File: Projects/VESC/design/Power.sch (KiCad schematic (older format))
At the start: 48 parts, among them U2 TC2117, U3 DRV8302

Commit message: More schematic updates for VESC
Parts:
- C1, C18, C19, C20, C21, C22, C23, C24, C26, C27, C28, C29, C30, C34, C36, C37, C39, C40, C43, C44, C49, C51, C52, C8, C9: symbol C-RESCUE-BLDC_4 -> C
- C25, C33: symbol CP1-RESCUE-BLDC_4 -> CP1
- D4: symbol DIODESCH -> D_Schottky
- D5: symbol DIODE -> D
- R17, R18, R19, R20, R21, R23, R24, R25, R26, R27, R32, R33, R48, R49, R50, R51: symbol R-RESCUE-BLDC_4 -> R
- U2: symbol NCP1117ST33T3G-RESCUE-BLDC_4 -> NCP1117ST33T3G
- U3: symbol DRV8302 -> DRV8302_1
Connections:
- net +5V: no longer U2.3 (VI)
- net GND: no longer U2.1 (GND)
- net VCC: no longer U2.2 (VO)
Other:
- moved on the sheet: U2

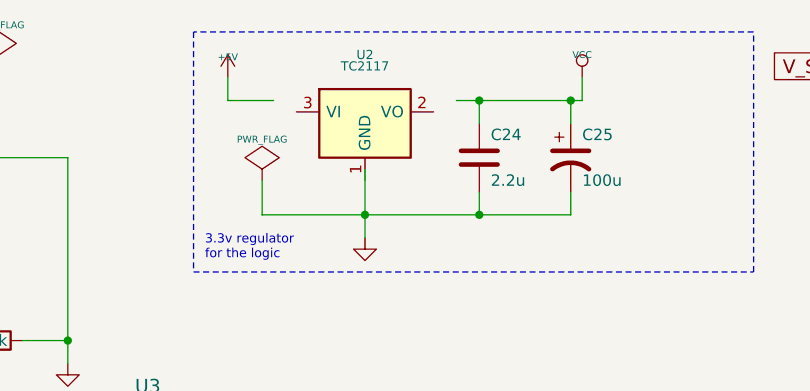
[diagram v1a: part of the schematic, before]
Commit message: VESC MOSFET layout
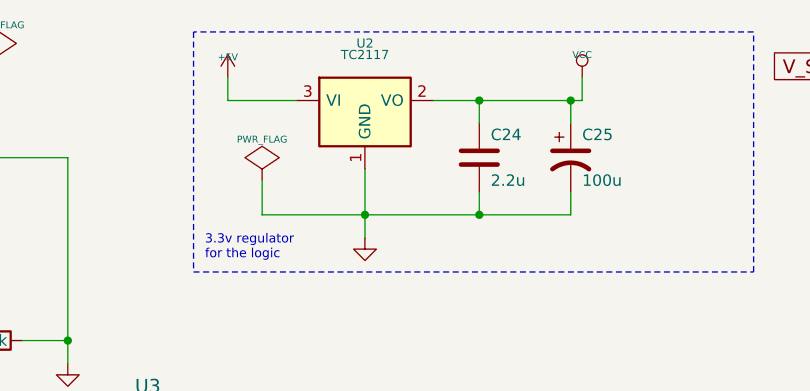
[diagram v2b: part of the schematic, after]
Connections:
- net +5V: now also U2.3 (VI)
- net GND: now also U2.1 (GND)
- net VCC: now also U2.2 (VO)
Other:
- moved on the sheet: U2
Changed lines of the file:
@@
 L NCP1117ST33T3G U2
 U 1 1 53E7AF36
-P 6300 1200
+P 6300 1150
 AR Path="/53E7AF36" Ref="U2"  Part="1"
 AR Path="/504F83BE/53E7AF36" Ref="U2"  Part="1"
-F 0 "U2" H 6300 1450 40  0000 C CNN
-F 1 "TC2117" H 6300 1400 40  0000 C CNN
-F 2 "CRF1:SOT-223" H 6300 1200 60  0001 C CNN
-F 3 "" H 6300 1200 60  0000 C CNN
-	1    6300 1200
+F 0 "U2" H 6300 1400 40  0000 C CNN
+F 1 "TC2117" H 6300 1350 40  0000 C CNN
+F 2 "CRF1:SOT-223" H 6300 1150 60  0001 C CNN
+F 3 "" H 6300 1150 60  0000 C CNN
+	1    6300 1150
 	1    0    0    -1
 $EndComp
@@
 0D 0D 85 50 5B 08 A1 71 E3 C6 45 47 47 77 AB F8 CD C0 F0 65 C3 18 9A 0F 4F 4B 4B 4B 51 51 51 53
 53 93 40 20 30 31 31 61 94 40 19 18 18 43 C3 C0 C0 A0 72 FE 07 CF 64 8C 61 E1 12 74 DD 00 00 00
-00 49 45 4E 44 AE 42 60 82 02
+00 49 45 4E 44 AE 42 60 82 17
 EndData
 $EndBitmap
@@
 A1 C7 18 00 00 C0 28 C8 B2 00 00 00 46 41 96 05 00 00 30 0A B2 2C 00 00 80 51 90 65 01 00 00 8C
 82 2C 0B 00 00 60 14 64 59 00 00 00 A3 FC 7F BD 9B 69 A6 C1 67 F0 EA 00 00 00 00 49 45 4E 44 AE
-42 60 82 37
+42 60 82 D7
 EndData
 $EndBitmap
@@
 AB D8 39 0B 59 91 9E DF A8 2A 5B EE 54 3A FD 71 ED 71 2F 29 C3 82 EC 80 87 06 6E C3 98 10 30 3B
 62 9A BB 2D 03 B8 C4 64 FC B5 26 AC 13 9B D1 39 40 41 C1 D6 78 4C 84 BF 94 F0 6F E1 BF 96 F0 0F
-FF 77 E2 FF 1F 0F 43 55 32 21 1C 08 16 00 00 00 00 49 45 4E 44 AE 42 60 82 0B
+FF 77 E2 FF 1F 0F 43 55 32 21 1C 08 16 00 00 00 00 49 45 4E 44 AE 42 60 82 04
 EndData
 $EndBitmap
@@
 Connection ~ 7200 1150
 Wire Wire Line
-	6700 1150 7250 1150
+	6600 1150 7250 1150
 Wire Wire Line
-	5900 1150 5700 1150
+	5700 1150 6000 1150
 Wire Wire Line
 	5700 1150 5700 1050

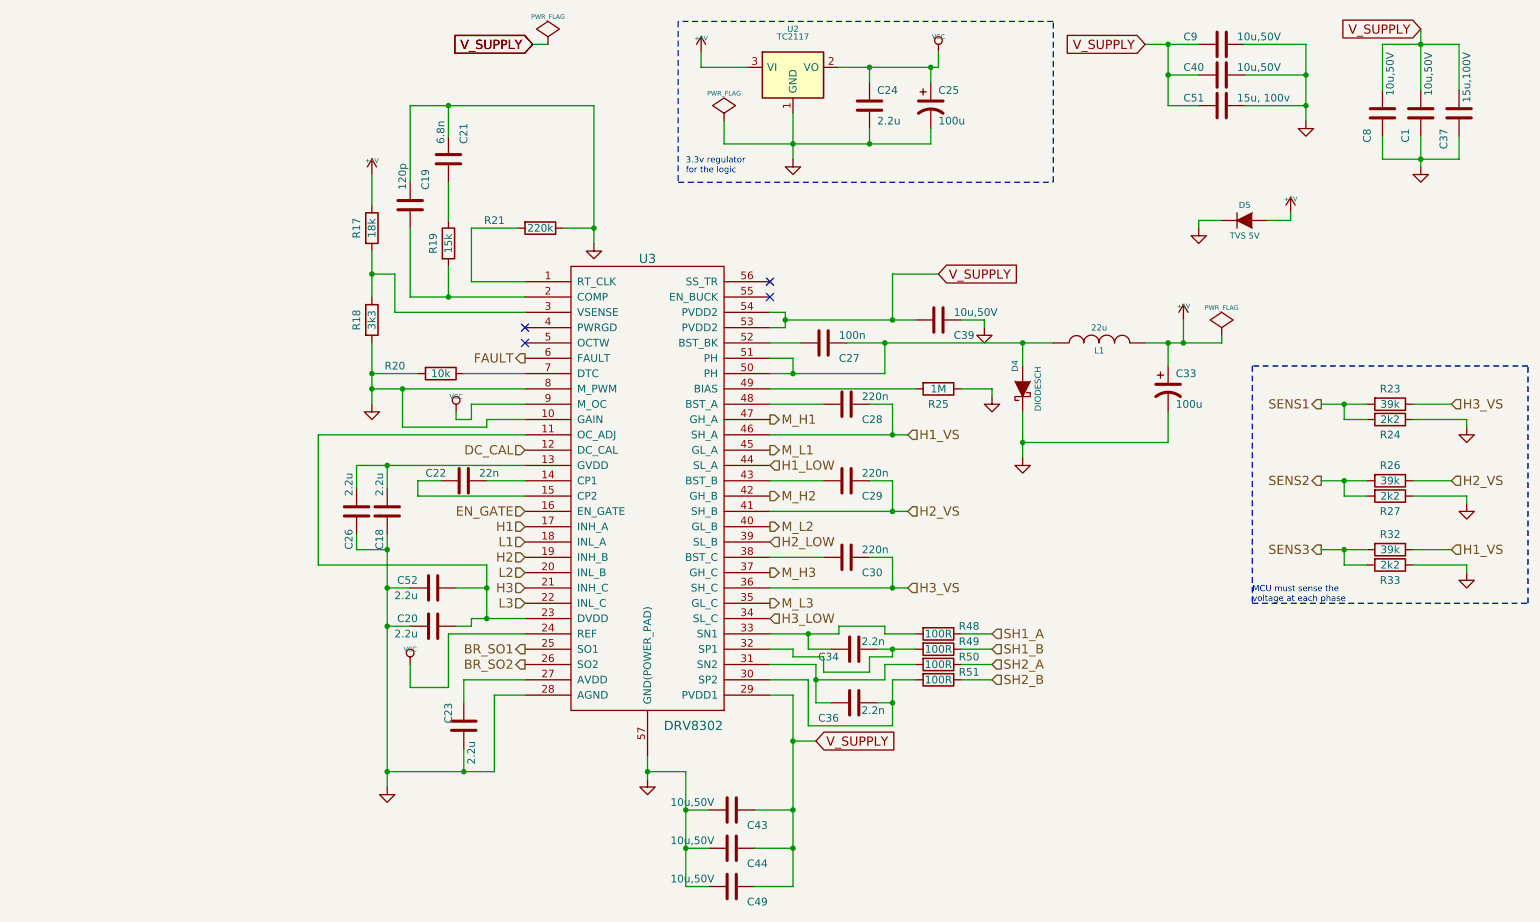
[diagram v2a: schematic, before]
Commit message: completing VESC card layout
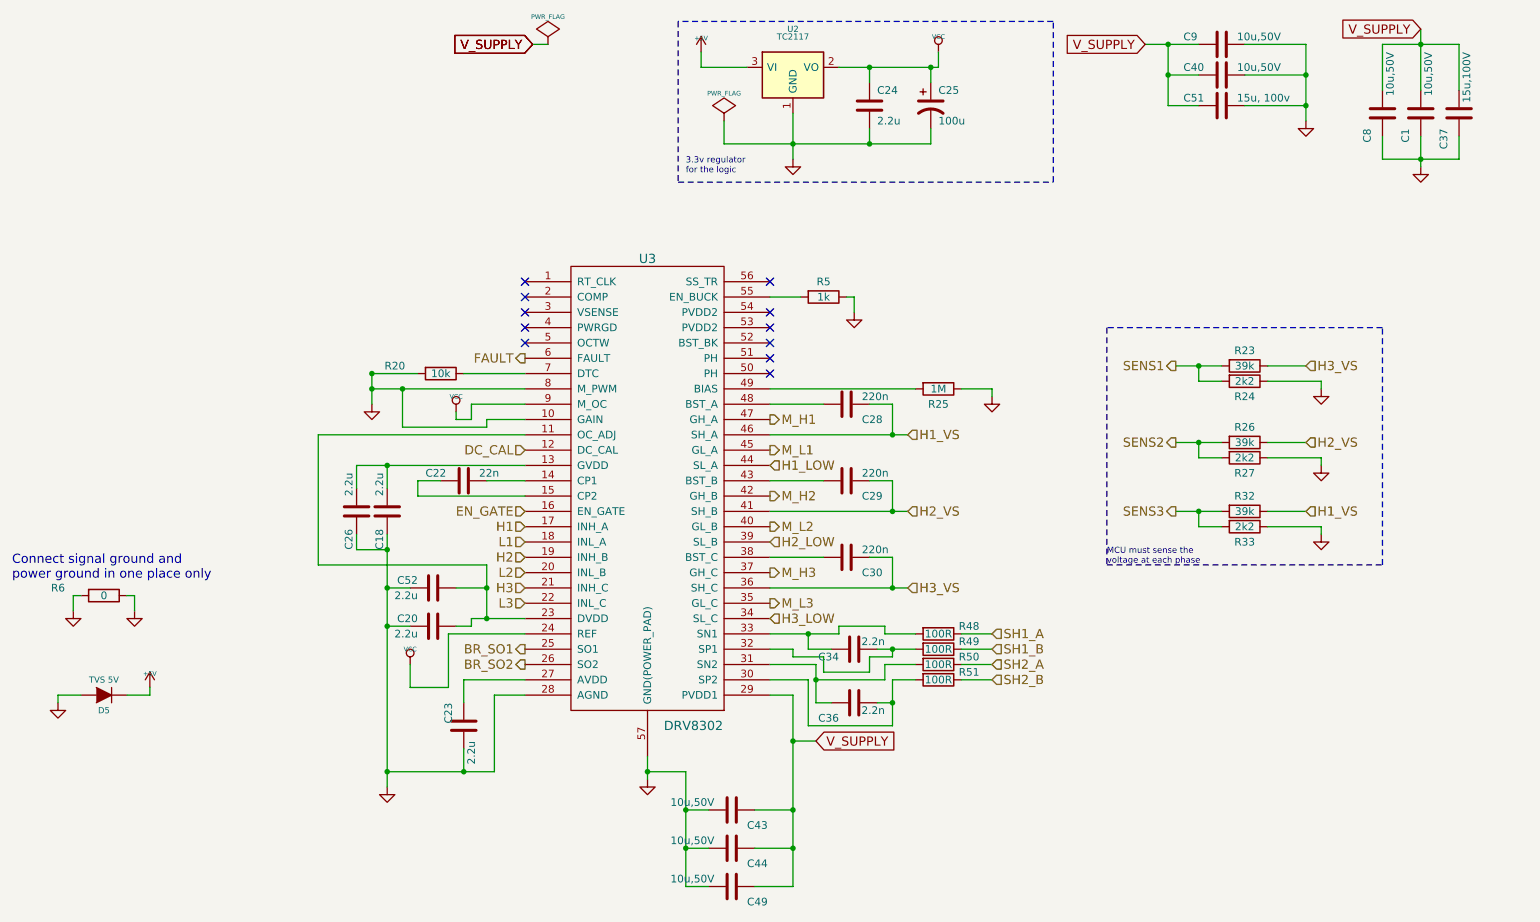
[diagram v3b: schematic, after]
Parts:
- removed C19: 120p, Capacitors_SMD:C_0805, symbol C
- removed C21: 6.8n, Capacitors_SMD:C_0805, symbol C
- removed C27: 100n, Capacitors_SMD:C_0805, symbol C
- removed C33: 100u, w_smd_cap:c_tant_B, symbol CP1
- removed C39: 10u,50V, CRF1:SMD-1206, symbol C
- removed D4: DIODESCH, Diodes_SMD:SMA_Handsoldering, symbol D_Schottky
- removed L1: 22u, w_smd_inductors:inductor_smd_8x5mm, symbol INDUCTOR
- removed R17: 18k, Resistors_SMD:R_0805, symbol R
- removed R18: 3k3, Resistors_SMD:R_0805, symbol R
- removed R19: 15k, Resistors_SMD:R_0805, symbol R
- removed R21: 220k, Resistors_SMD:R_0805, symbol R
- added R5: 1k, Resistors_SMD:R_0805, symbol R
- added R6: 0, Resistors_SMD:R_1210, symbol R
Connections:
- net +5V: now also D5.1 (K); no longer D5.2 (A)
- net GND: now also R5.1, R6.2; no longer C18.2, C20.1, C23.1, C24.2, C25.2, C26.2, C52.1, D5.1 (K), R20.2, R24.1, R27.1, R33.1, U2.1 (GND), U3.10 (GAIN), U3.28 (AGND), U3.8 (M_PWM)
- net V_SUPPLY: no longer U3.53 (PVDD2), U3.54 (PVDD2)
- net at U3.50 (PH): no longer U3.51 (PH)
- net at U3.55 (EN_BUCK): now also R5.2
- new net GNDD: C18.2, C20.1, C23.1, C24.2, C25.2, C26.2, C52.1, D5.2 (A), R20.2, R24.1, R27.1, R33.1, R6.1, U2.1 (GND), U3.10 (GAIN), U3.28 (AGND), U3.8 (M_PWM)
- no-connect marks 4 -> 11
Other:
- note added: "Connect signal ground and\npower ground in one place only"
- moved on the sheet: D5, R23, R24, R26, R27, R32, R33

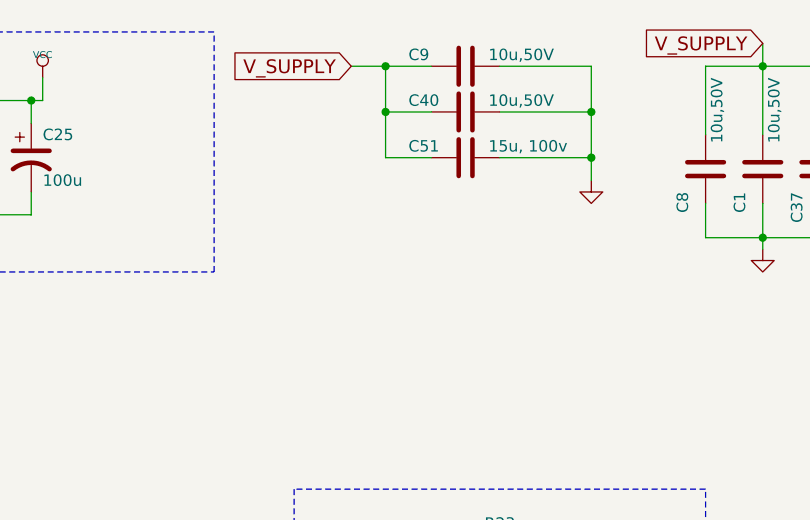
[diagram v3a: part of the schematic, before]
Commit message: Ground plane and silkscreen of VESC-R
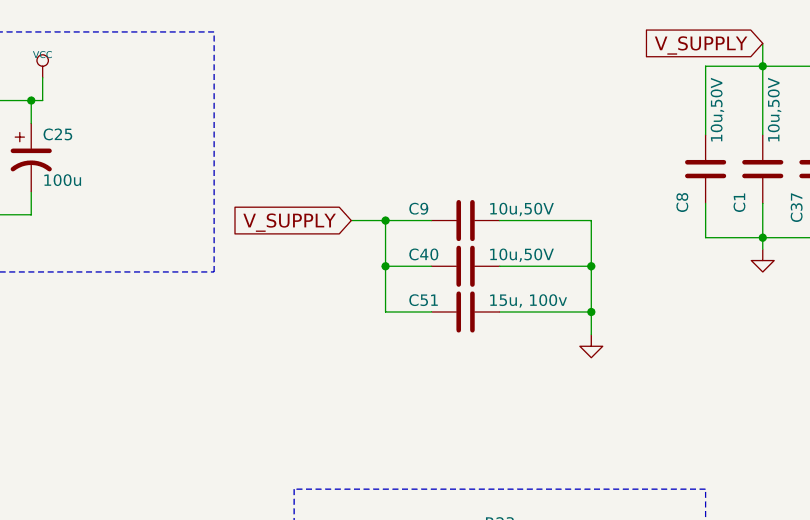
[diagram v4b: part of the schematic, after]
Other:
- moved on the sheet: C40, C51, C9
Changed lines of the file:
@@
 L C C51
 U 1 1 51094370
-P 9100 1400
-F 0 "C51" V 9050 1150 50  0000 L CNN
-F 1 "15u, 100v" V 9050 1500 50  0000 L CNN
-F 2 "w_smd_cap:c_2220" H 9100 1400 60  0001 C CNN
-F 3 "" H 9100 1400 60  0001 C CNN
-	1    9100 1400
+P 9100 2075
+F 0 "C51" V 9050 1825 50  0000 L CNN
+F 1 "15u, 100v" V 9050 2175 50  0000 L CNN
+F 2 "w_smd_cap:c_2220" H 9100 2075 60  0001 C CNN
+F 3 "" H 9100 2075 60  0001 C CNN
+	1    9100 2075
 	0    1    1    0
 $EndComp
@@
 L GND #PWR054
 U 1 1 510944D0
-P 9650 1500
-F 0 "#PWR054" H 9650 1500 30  0001 C CNN
-F 1 "GND" H 9650 1430 30  0001 C CNN
-F 2 "" H 9650 1500 60  0001 C CNN
-F 3 "" H 9650 1500 60  0001 C CNN
-	1    9650 1500
+P 9650 2175
+F 0 "#PWR054" H 9650 2175 30  0001 C CNN
+F 1 "GND" H 9650 2105 30  0001 C CNN
+F 2 "" H 9650 2175 60  0001 C CNN
+F 3 "" H 9650 2175 60  0001 C CNN
+	1    9650 2175
 	1    0    0    -1
 $EndComp
@@
 L C C40
 U 1 1 53E7AF97
-P 9100 1200
-F 0 "C40" V 9050 950 50  0000 L CNN
-F 1 "10u,50V" V 9050 1300 50  0000 L CNN
-F 2 "CRF1:SMD-1206" H 9100 1200 60  0001 C CNN
-F 3 "" H 9100 1200 60  0001 C CNN
-	1    9100 1200
+P 9100 1875
+F 0 "C40" V 9050 1625 50  0000 L CNN
+F 1 "10u,50V" V 9050 1975 50  0000 L CNN
+F 2 "CRF1:SMD-1206" H 9100 1875 60  0001 C CNN
+F 3 "" H 9100 1875 60  0001 C CNN
+	1    9100 1875
 	0    1    1    0
 $EndComp
@@
 L C C9
 U 1 1 53E7AFA2
-P 9100 1000
-F 0 "C9" V 9050 750 50  0000 L CNN
-F 1 "10u,50V" V 9050 1100 50  0000 L CNN
-F 2 "CRF1:SMD-1206" H 9100 1000 60  0001 C CNN
-F 3 "" H 9100 1000 60  0001 C CNN
-	1    9100 1000
+P 9100 1675
+F 0 "C9" V 9050 1425 50  0000 L CNN
+F 1 "10u,50V" V 9050 1775 50  0000 L CNN
+F 2 "CRF1:SMD-1206" H 9100 1675 60  0001 C CNN
+F 3 "" H 9100 1675 60  0001 C CNN
+	1    9100 1675
 	0    1    1    0
 $EndComp
@@
 0D 0D 85 50 5B 08 A1 71 E3 C6 45 47 47 77 AB F8 CD C0 F0 65 C3 18 9A 0F 4F 4B 4B 4B 51 51 51 53
 53 93 40 20 30 31 31 61 94 40 19 18 18 43 C3 C0 C0 A0 72 FE 07 CF 64 8C 61 E1 12 74 DD 00 00 00
-00 49 45 4E 44 AE 42 60 82 01
+00 49 45 4E 44 AE 42 60 82 00
 EndData
 $EndBitmap
@@
 A1 C7 18 00 00 C0 28 C8 B2 00 00 00 46 41 96 05 00 00 30 0A B2 2C 00 00 80 51 90 65 01 00 00 8C
 82 2C 0B 00 00 60 14 64 59 00 00 00 A3 FC 7F BD 9B 69 A6 C1 67 F0 EA 00 00 00 00 49 45 4E 44 AE
-42 60 82 45
+42 60 82 2C
 EndData
 $EndBitmap
@@
 AB D8 39 0B 59 91 9E DF A8 2A 5B EE 54 3A FD 71 ED 71 2F 29 C3 82 EC 80 87 06 6E C3 98 10 30 3B
 62 9A BB 2D 03 B8 C4 64 FC B5 26 AC 13 9B D1 39 40 41 C1 D6 78 4C 84 BF 94 F0 6F E1 BF 96 F0 0F
-FF 77 E2 FF 1F 0F 43 55 32 21 1C 08 16 00 00 00 00 49 45 4E 44 AE 42 60 82 0A
+FF 77 E2 FF 1F 0F 43 55 32 21 1C 08 16 00 00 00 00 49 45 4E 44 AE 42 60 82 16
 EndData
 $EndBitmap
@@
 $EndComp
 NoConn ~ 6150 2550
-Text GLabel 8600 1000 0    60   Input ~ 0
+Text GLabel 8600 1675 0    60   Input ~ 0
 V_SUPPLY
 $Comp
@@
 	6300 6500 6050 6500
 Wire Wire Line
-	9650 1400 9250 1400
+	9650 2075 9250 2075
 Wire Wire Line
-	9650 1000 9650 1500
+	9650 1675 9650 2175
 Wire Wire Line
 	3650 4550 3800 4550
@@
 Connection ~ 4300 4750
 Wire Wire Line
-	8750 1000 8750 1400
+	8750 1675 8750 2075
 Wire Wire Line
-	8750 1400 8950 1400
+	8750 2075 8950 2075
 Wire Wire Line
-	8750 1200 8950 1200
-Connection ~ 8750 1200
+	8750 1875 8950 1875
+Connection ~ 8750 1875
 Wire Wire Line
-	8600 1000 8950 1000
-Connection ~ 8750 1000
-Connection ~ 9650 1400
+	8600 1675 8950 1675
+Connection ~ 8750 1675
+Connection ~ 9650 2075
 Wire Wire Line
-	9250 1000 9650 1000
+	9250 1675 9650 1675
 Wire Wire Line
-	9250 1200 9650 1200
-Connection ~ 9650 1200
+	9250 1875 9650 1875
+Connection ~ 9650 1875
 Wire Notes Line
 	8350 2850 8350 4400
